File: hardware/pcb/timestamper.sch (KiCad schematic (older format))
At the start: 110 parts, among them J1 Conn_Coaxial, J2 Conn_Coaxial, J3 Conn_Coaxial, J4 JTAG, J5 ISP, J6 Conn_Coaxial, J7 USB_B_Micro, U1 AP1117-33, U10 ATMEGA328-AU, U11 74HC04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

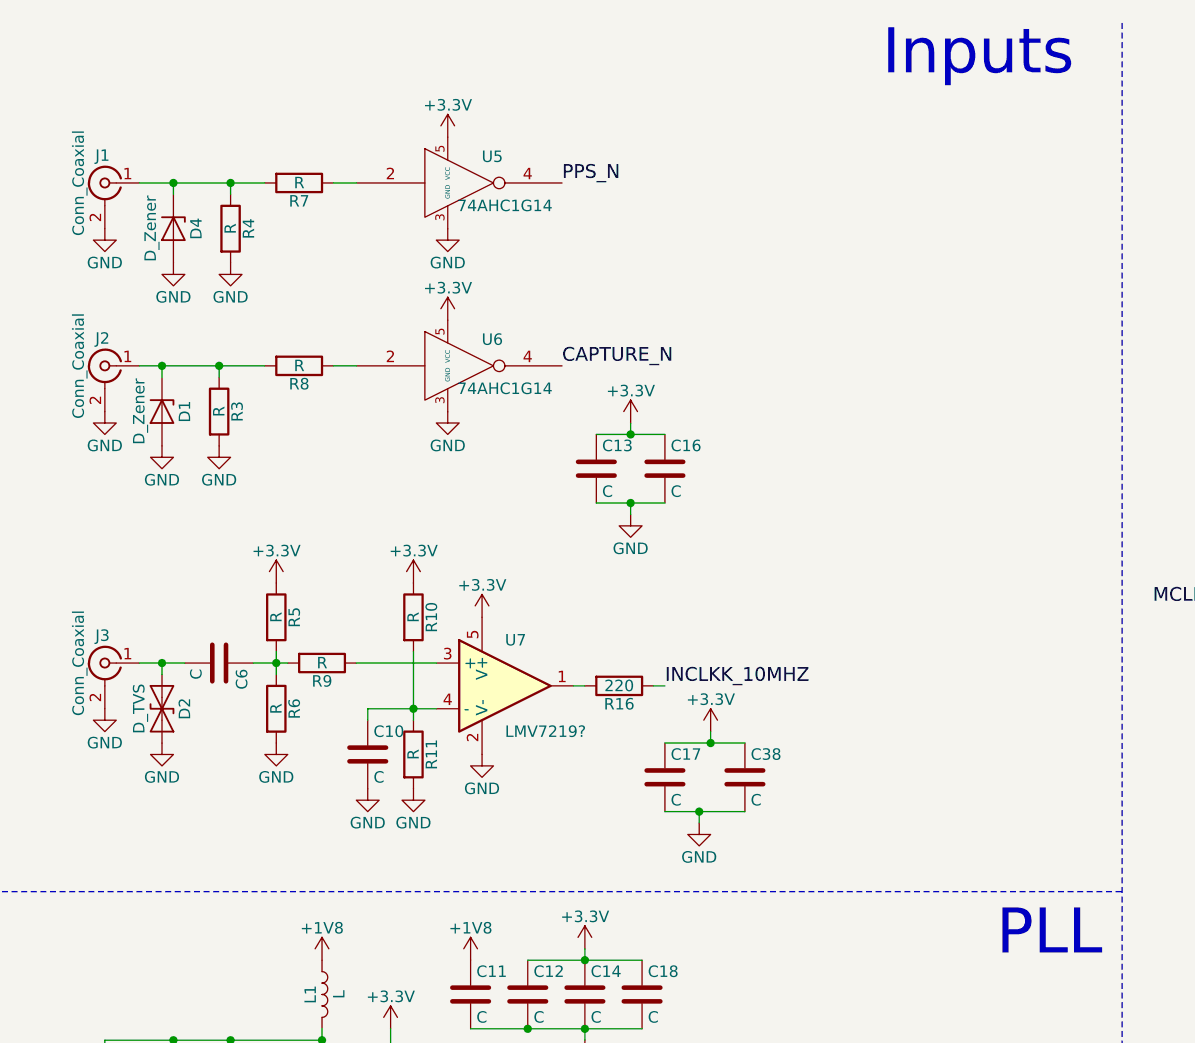
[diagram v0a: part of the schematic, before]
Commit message: Added optional schmitt input on refclk
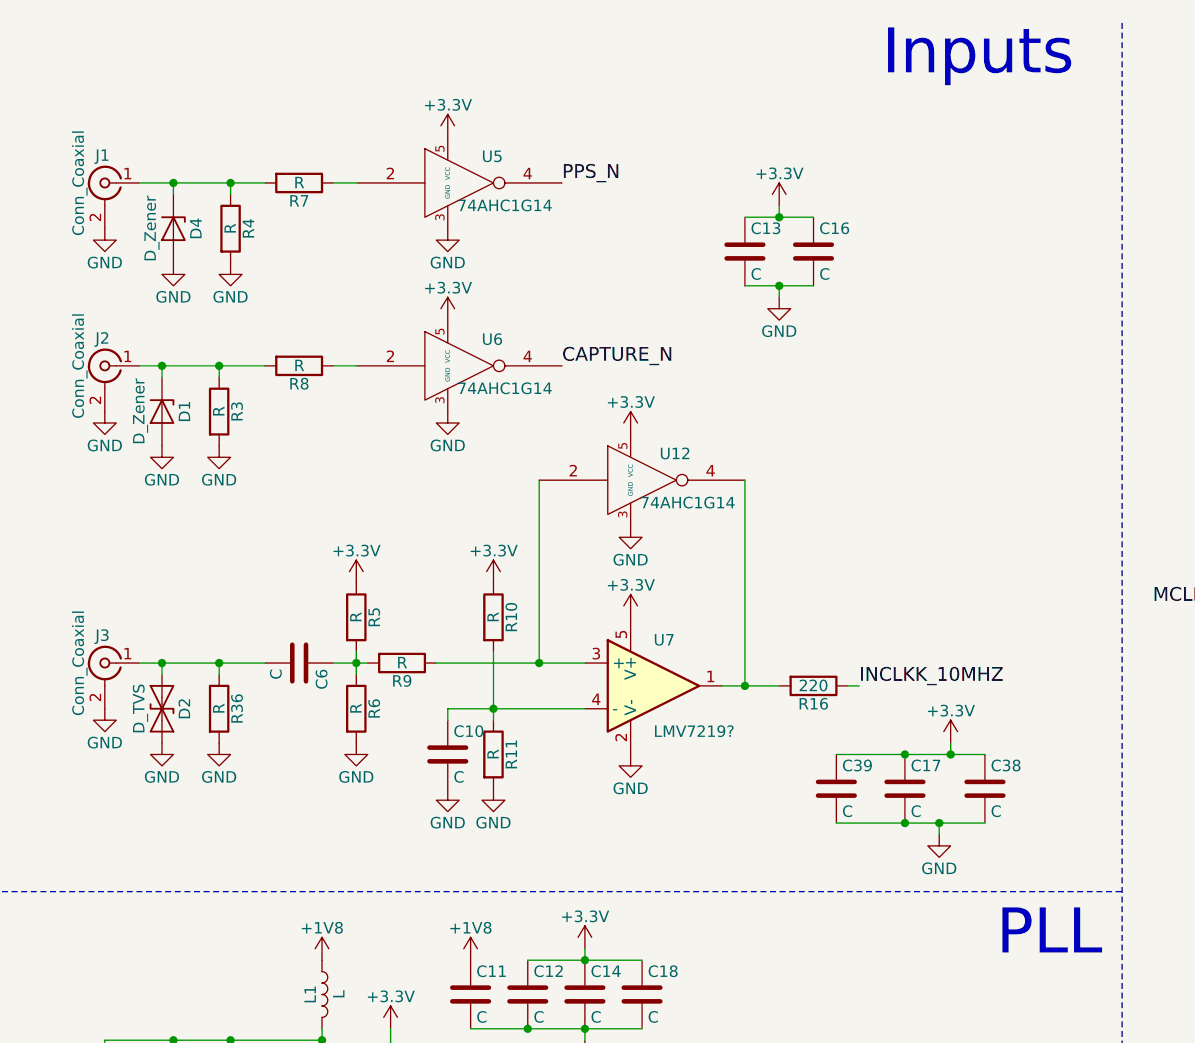
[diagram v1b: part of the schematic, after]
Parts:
- added C39: C, Capacitor_SMD:C_0603_1608Metric, symbol timestamper-rescue:C
- added R36: R, Resistor_SMD:R_0603_1608Metric, symbol timestamper-rescue:R
- added U12: 74AHC1G14, Package_TO_SOT_SMD:SOT-353_SC-70-5, symbol timestamper-rescue:74AHC1G14
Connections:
- net +3V3: now also C39.1, U12.5 (VCC)
- net GND: now also C39.2, R36.2, U12.3 (GND)
- net at R16.2, U7.1: now also U12.4
- net at R9.1, U7.3 (+): now also U12.2
- net at C6.2, D2.1 (A1), J3.1 (In): now also R36.1
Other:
- moved on the sheet: C10, C13, C16, C17, C38, C6, R10, R11, R16, R5, R6, R9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

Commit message: Added optional schmitt input on refclk
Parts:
- C1, C10, C11, C12, C13, C14, C16, C17, C18, C22, C24, C26, C27, C29, C30, C31, C33, C34, C38, C39, C4, C5: value C -> 100n
- C15, C19, C36, C37: value C -> 22p
- C25, C28, C32, C9: value C -> 10n
- C35: value C -> 1u
- C7: footprint Capacitor_SMD:C_0603_1608Metric -> Capacitor_SMD:C_0805_2012Metric
- D1, D4: value D_Zener -> PESD5V2S2UT; footprint Diode_SMD:D_SOT-23_ANK -> Diode_SMD:D_SOT-23_NKA
- D2: value D_TVS -> PESD5V0U2BTTVS
- D3: value D_Zener -> 5v6
- D7: value D_Zener -> PESD3V3S2UT; footprint Diode_SMD:D_SOT-23_ANK -> Diode_SMD:D_SOT-23_NKA
- R1, R10, R11, R18, R19: value R -> 10k
- R12, R13, R15: value R -> 33
- R14, R17, R5, R6, R7, R8, R9: value R -> 100
- R20: value R -> 100k
- R22, R23, R24, R25, R26, R27: value R -> 270
- R28, R29, R30, R31, R32, R33: value R -> 330
- R3, R4: value R -> 51
- R34, R35: value R -> 2k2
- R36: value R -> 51; footprint Resistor_SMD:R_0603_1608Metric -> Resistor_SMD:R_0805_2012Metric
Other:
- note added: "* Schmitt trigger by Nexperia."

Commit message: Small fixes
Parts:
- added C40: 0, Capacitor_SMD:C_0603_1608Metric, symbol timestamper-rescue:C
- U12, U5, U6: value 74AHC1G14 -> 74LVC1G14
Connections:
- net GND: now also C40.2
- net MCLK_100MHZ: now also C40.1
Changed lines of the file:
@@
 P 2550 1200
 F 0 "U5" H 2695 1315 50  0000 C CNN
-F 1 "74AHC1G14" H 2750 1100 50  0000 C CNN
+F 1 "74LVC1G14" H 2750 1100 50  0000 C CNN
 F 2 "Package_TO_SOT_SMD:SOT-353_SC-70-5" H 2645 1065 50  0001 C CNN
 F 3 "" H 2695 1315 50  0001 C CNN
@@
 P 2550 2000
 F 0 "U6" H 2695 2115 50  0000 C CNN
-F 1 "74AHC1G14" H 2750 1900 50  0000 C CNN
+F 1 "74LVC1G14" H 2750 1900 50  0000 C CNN
 F 2 "Package_TO_SOT_SMD:SOT-353_SC-70-5" H 2645 1865 50  0001 C CNN
 F 3 "" H 2695 2115 50  0001 C CNN
@@
 Text Label 7650 3950 3    60   ~ 0
 CPLD_CE_N
-Text Label 6750 3200 2    60   ~ 0
+Text Label 6200 3200 2    60   ~ 0
 CPLD_RST_CAPT
 Text Label 7800 3950 3    60   ~ 0
@@
 LED_D9
 Wire Wire Line
-	6200 3050 6750 3050
+	6200 3050 6400 3050
 Connection ~ 6800 6400
 Wire Notes Line
@@
 P 3350 2500
 F 0 "U12" H 3495 2615 50  0000 C CNN
-F 1 "74AHC1G14" H 3550 2400 50  0000 C CNN
+F 1 "74LVC1G14" H 3550 2400 50  0000 C CNN
 F 2 "Package_TO_SOT_SMD:SOT-353_SC-70-5" H 3445 2365 50  0001 C CNN
 F 3 "" H 3495 2615 50  0001 C CNN
@@
 Text Notes 3800 2550 0    50   ~ 0
 * Schmitt trigger by Nexperia.
+$Comp
+L timestamper-rescue:C C40
+U 1 1 5C8EF151
+P 6400 3500
+F 0 "C40" H 6425 3600 50  0000 L CNN
+F 1 "0" H 6425 3400 50  0000 L CNN
+F 2 "Capacitor_SMD:C_0603_1608Metric" H 6438 3350 50  0001 C CNN
+F 3 "" H 6400 3500 50  0001 C CNN
+	1    6400 3500
+	1    0    0    -1
+$EndComp
+Wire Wire Line
+	6200 3200 6750 3200
+Wire Wire Line
+	6400 3350 6400 3050
+Connection ~ 6400 3050
+Wire Wire Line
+	6400 3050 6750 3050
+$Comp
+L power:GND #PWR0103
+U 1 1 5C90E89E
+P 6400 3650
+F 0 "#PWR0103" H 6400 3400 50  0001 C CNN
+F 1 "GND" H 6400 3500 50  0000 C CNN
+F 2 "" H 6400 3650 50  0001 C CNN
+F 3 "" H 6400 3650 50  0001 C CNN
+	1    6400 3650
+	1    0    0    -1
+$EndComp
 $EndSCHEMATC
